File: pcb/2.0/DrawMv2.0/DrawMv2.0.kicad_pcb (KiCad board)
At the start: 2 copper layers, 97.5 x 67.3 mm, 43 parts, among them J1 M1, J10 debug, J11 Conn_01x03_Pin, J2 M2, J3 M3, J4 PWR, J5 X_SW, J6 Y_SW, J7 Z_SW, J8 Conn_01x03_Pin, J9 Conn_01x04_Pin

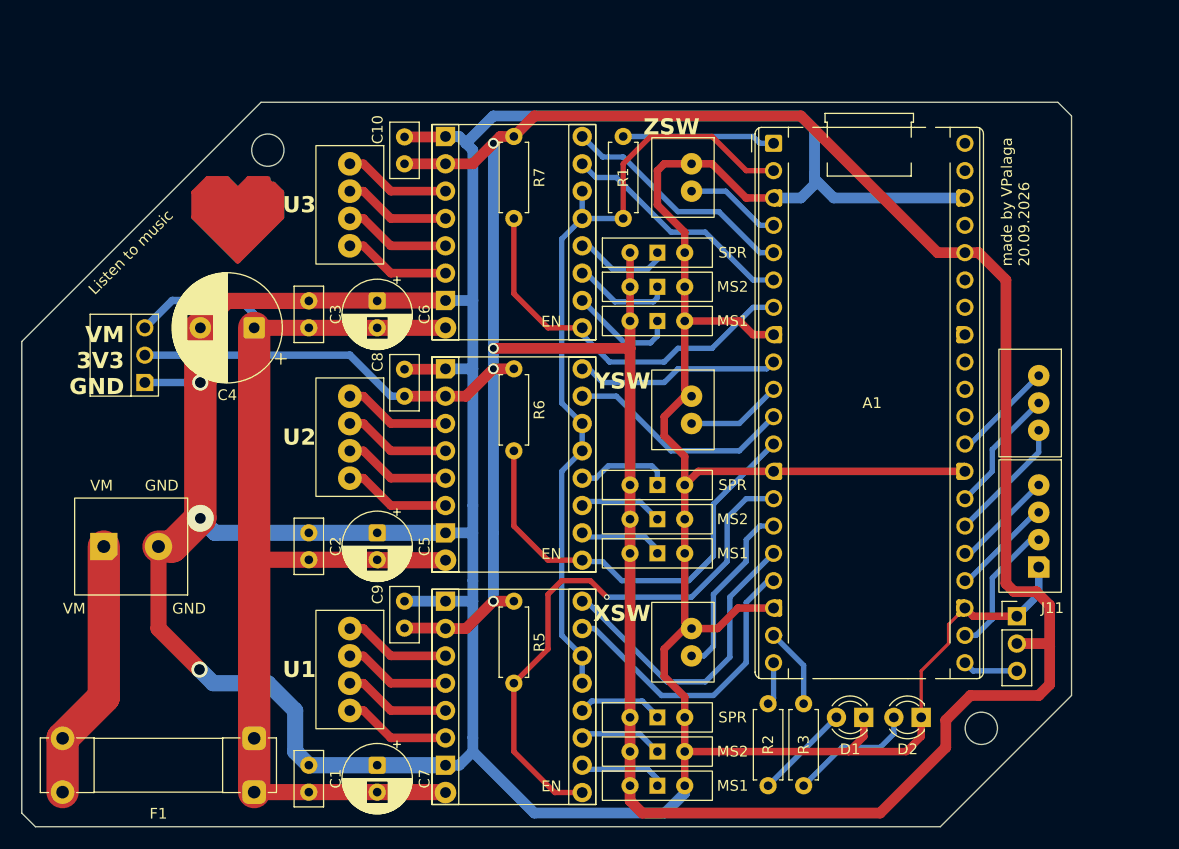
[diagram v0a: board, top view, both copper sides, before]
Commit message: separate the head driver
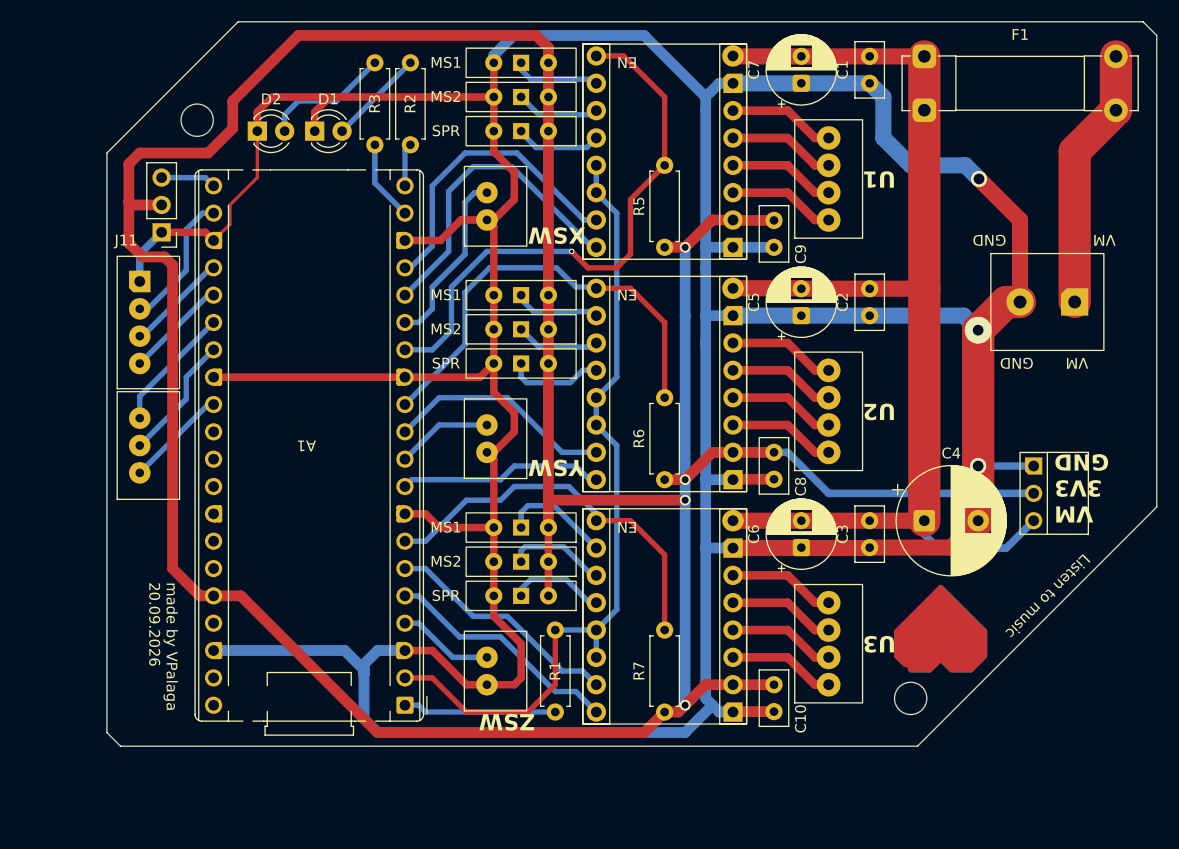
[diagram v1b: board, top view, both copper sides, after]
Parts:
- moved F1 92.5 mm to (171.5, 66.9), turned to 0 degrees
- moved J4 88.1 mm to (182.9, 89.7), turned to 0 degrees
- moved J11 87.1 mm to (100.6, 83.2), turned to 180 degrees
- moved J9 85.1 mm to (98.6, 92.8), turned to 90 degrees
- moved J8 83.6 mm to (98.6, 103.0), turned to 90 degrees
- moved J10 83.6 mm to (181.7, 107.5), turned to 90 degrees
- moved D2 82.3 mm to (109.5, 73.8), turned to 0 degrees
- moved C1 82.0 mm to (166.4, 69.4), turned to 90 degrees
- moved D1 74.6 mm to (114.8, 73.8), turned to 0 degrees
- moved C7 74.6 mm to (160.1, 69.4), turned to 90 degrees
- moved MS1 68.4 mm to (134.0, 67.5), turned to 180 degrees
- moved R3 65.5 mm to (120.4, 75.1), turned to 90 degrees
- moved C4 64.8 mm to (171.5, 110.0), turned to 0 degrees
- moved A1 62.4 mm to (123.2, 127.1), turned to 180 degrees
- moved MS2 62.1 mm to (134.0, 70.6), turned to 180 degrees
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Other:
- outline, holes or cut-outs redrawn
